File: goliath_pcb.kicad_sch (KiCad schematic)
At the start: 95 parts, among them IC1 MCT9001, IC2 MCT9001, IC3 MCT9001, IC4 MCT9001, IC5 MCT9001, IC6 MCT9001, IC7 MCT9001, J1 RJ45_LED, J10 Conn_01x04_Male, J11 Screw_Terminal_01x02, J12 Screw_Terminal_01x02, J13 Screw_Terminal_01x02, J14 Conn_01x02_Male, J15 Conn_01x02_Male, J2 RJ45_LED, J3 RJ45_LED, J4 RJ45_LED, J5 Conn_01x08_Male, J6 Conn_01x08_Male, J7 Conn_01x02_Male, J8 Conn_01x04_Male, J9 Conn_01x04_Male, Q1 STP2N80K5, Q2 STP2N80K5, U1 Pico, U2 LM2592HVT-5.0/NOPB, U3 74HCT244, U4 74HCT244, U5 MCP3008, U6 PCF8574, U7 PCF8574

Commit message: Clean up schematic
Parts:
- renumbered IC1 to OC1, IC2 to OC2, IC3 to OC3, IC4 to OC4, IC5 to OC5, IC6 to OC6, IC7 to OC7
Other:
- note removed: "LOW EMR caps closest to osmc as possible"
- moved on the sheet: C1, C6, C7, D1, D2, D3, D4, D7, D8, J1, J10, J11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

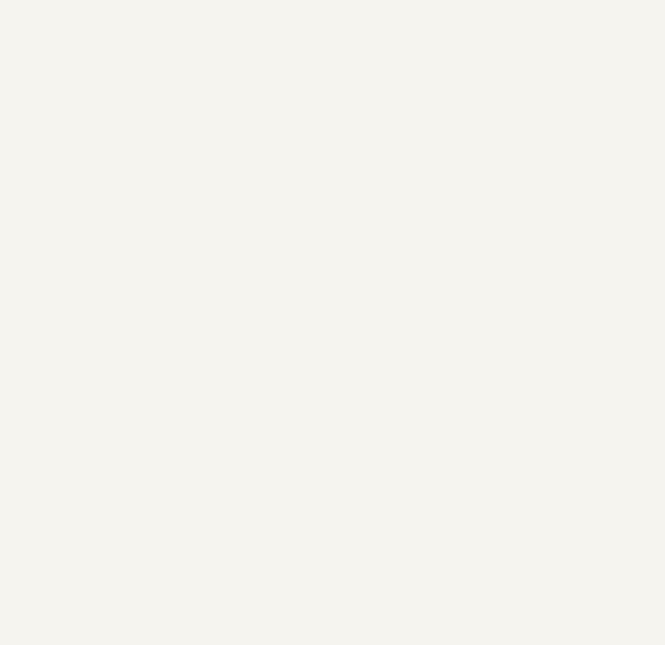
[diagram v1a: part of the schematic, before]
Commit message: Add proper M4 mounting holes
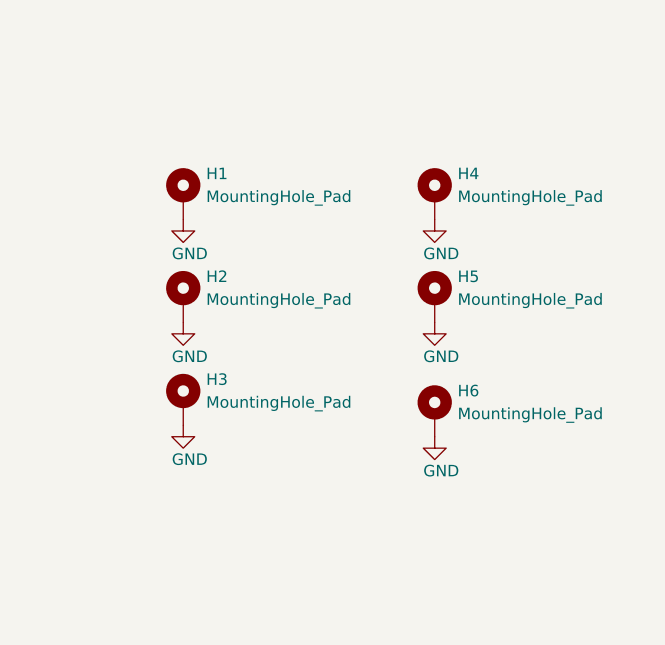
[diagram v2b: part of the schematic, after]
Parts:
- added H1, H2, H3, H4, H5, H6: MountingHole_Pad, MountingHole:MountingHole_4.3mm_M4_Pad_Via, symbol Mechanical:MountingHole_Pad
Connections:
- net GND: now also H1.1, H2.1, H3.1, H4.1, H5.1, H6.1

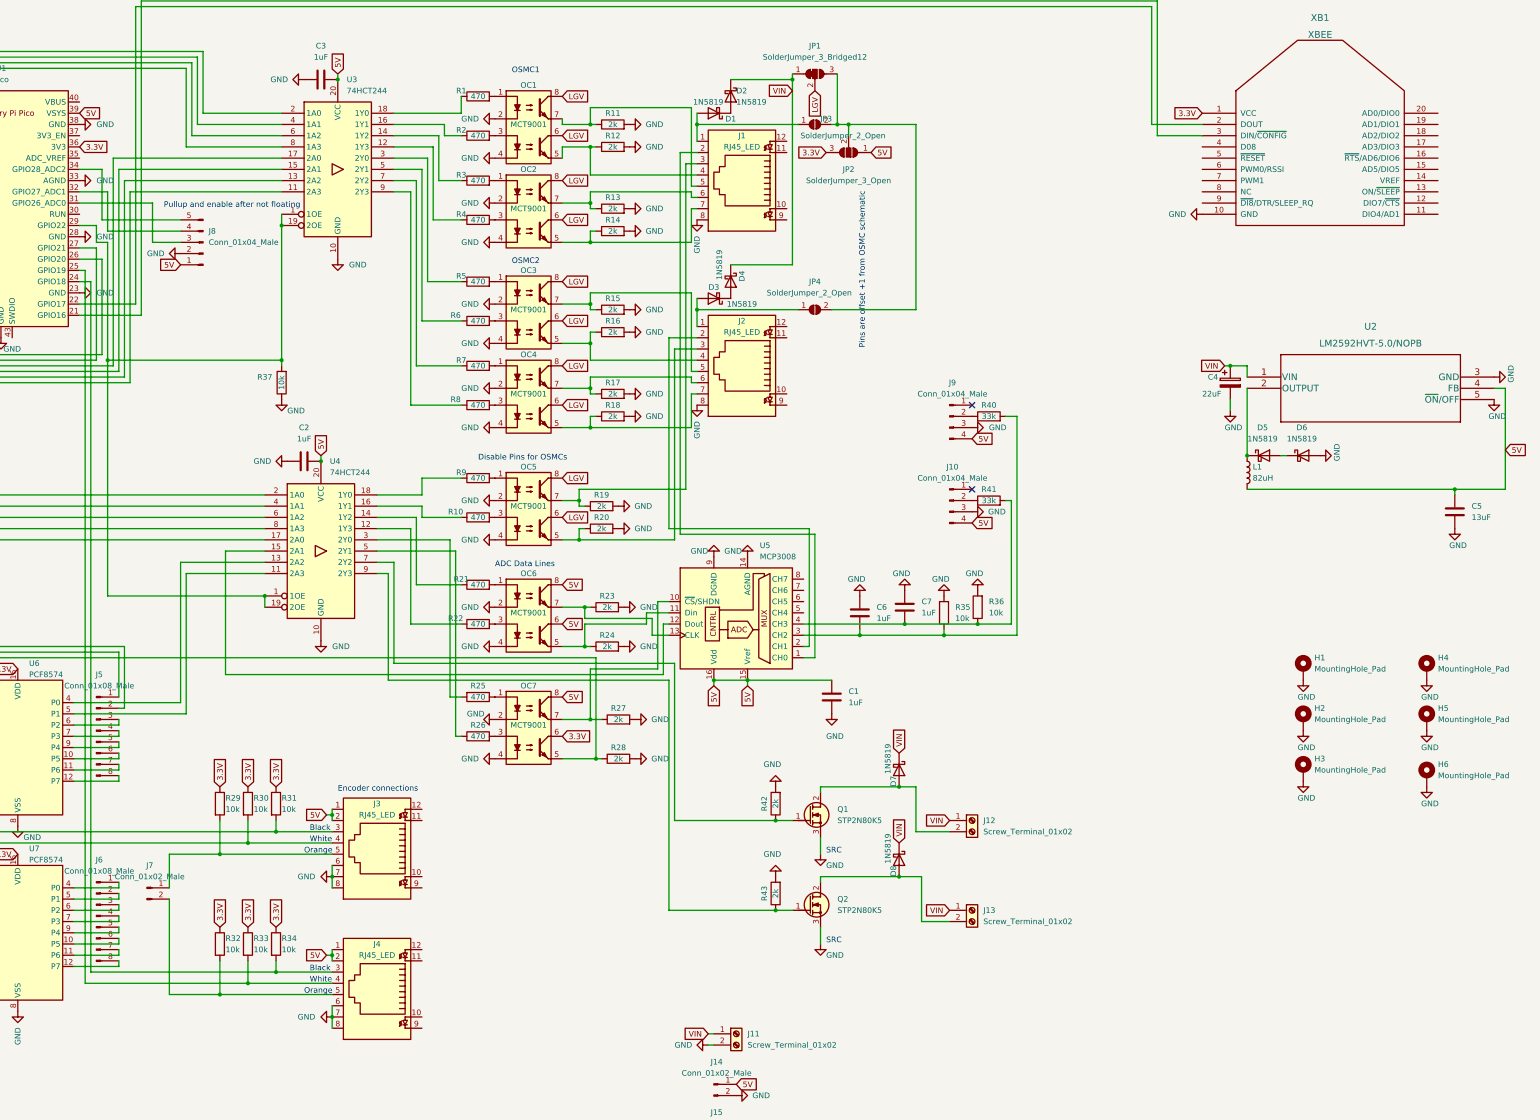
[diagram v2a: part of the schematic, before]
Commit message: Switch to better diodes, use via stitching plugin
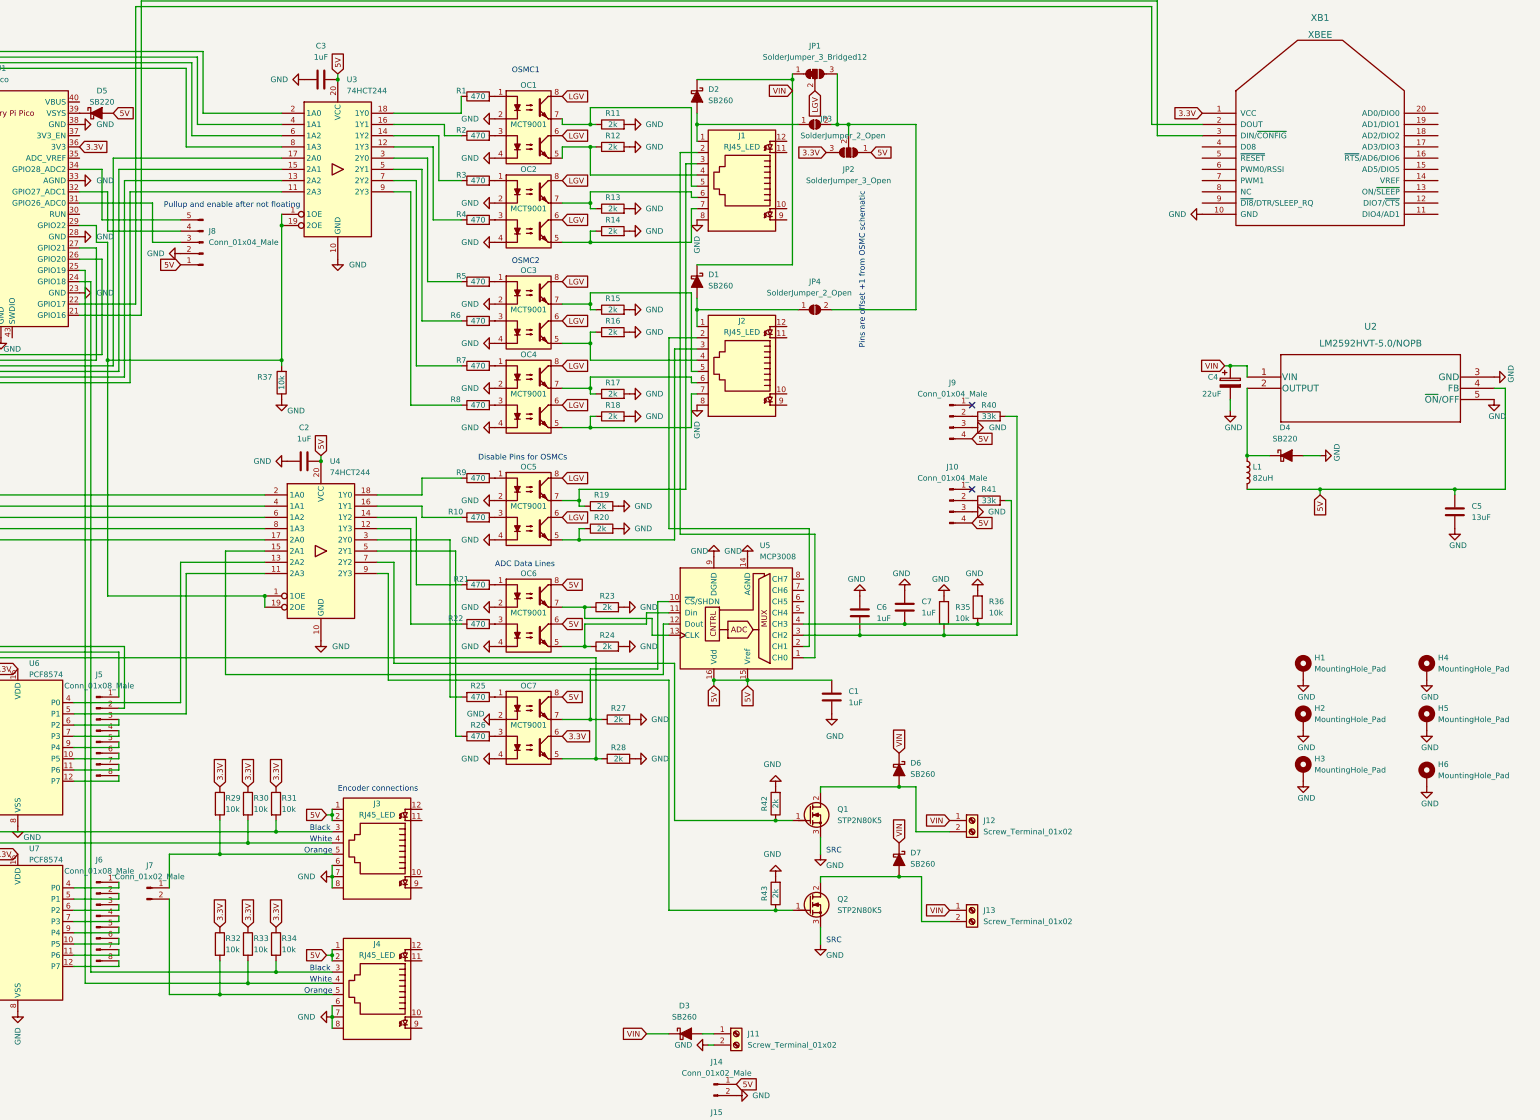
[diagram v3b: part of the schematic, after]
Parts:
- removed D1, D2, D3, D4, D5, D6, D7, D8: 1N5819, Diode_THT:D_DO-41_SOD81_P10.16mm_Horizontal, symbol Diode:1N5819
- added D1, D2, D3, D6, D7: SB260, Diode_THT_AKL:D_DO-15_P10.16mm_Horizontal, symbol Diode_Schottky_AKL:SB260
- added D4, D5: SB220, Diode_THT_AKL:D_DO-15_P10.16mm_Horizontal, symbol Diode_Schottky_AKL:SB220
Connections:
- net 5V: now also D5.2 (A); no longer U1.39 (VSYS)
- net GND: now also D4.2 (A)
- net VIN: now also D1.1 (K), D2.1 (K), D3.1 (K), D6.1 (K), D7.1 (K); no longer J11.1 (Pin_1)
- net at J12.2 (Pin_2), Q1.2 (D): now also D6.2 (A)
- net at J13.2 (Pin_2), Q2.2 (D): now also D7.2 (A)
- net at J1.1, JP3.1 (A): now also D2.2 (A)
- net at L1.1, U2.2 (OUTPUT): now also D4.1 (K)
- net at J2.1, JP4.1 (A): now also D1.2 (A)
- new net: D3.2 (A), J11.1 (Pin_1)
- new net: D5.1 (K), U1.39 (VSYS)

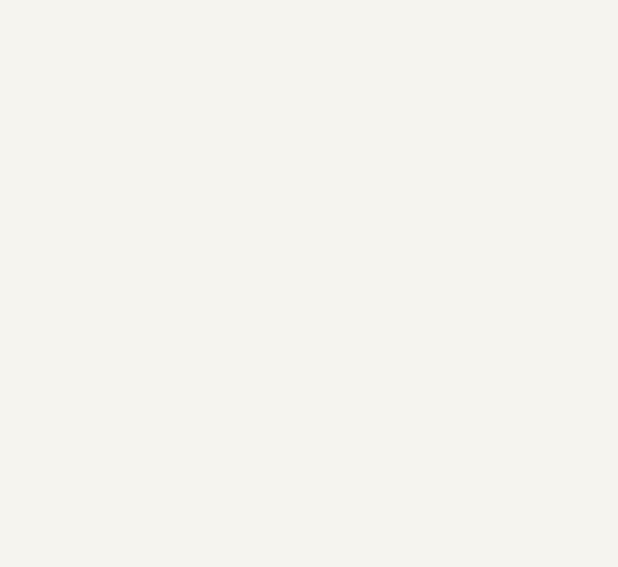
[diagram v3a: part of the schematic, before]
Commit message: Adjust via stitching to alighn with silkscreen text
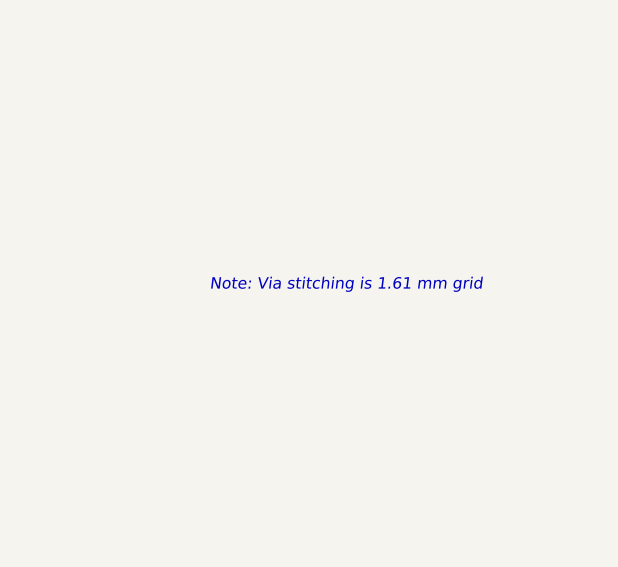
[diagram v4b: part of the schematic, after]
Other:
- note added: "Note: Via stitching is 1.61 mm grid"
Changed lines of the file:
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@@
     (effects (font (size 1.27 1.27)) (justify left bottom))
+  )
+  (text "Note: Via stitching is 1.61 mm grid" (at 370.84 246.38 0)
+    (effects (font (size 1.27 1.27) italic) (justify left bottom))
   )
   (text "Pins are offset +1 from OSMC schematic" (at 250.19 62.23 270)

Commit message: BIG inductor
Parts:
- C4: footprint Capacitor_THT:C_Rect_L7.0mm_W4.5mm_P5.00mm -> Capacitor_THT:CP_Radial_D5.0mm_P2.50mm
- C5: value 13uF -> 10uF
- L1: value 82uH -> 120uH; footprint Inductor_THT:L_Axial_L6.6mm_D2.7mm_P10.16mm_Horizontal_Vishay_IM-2 -> Inductor_THT_AKL:L_Radial_D12.5mm_P7.00mm_Fastron_09HCP
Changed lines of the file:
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@@
       (effects (font (size 1.27 1.27)) (justify left))
     )
-    (property "Value" "82uH" (id 1) (at 337.82 126.9999 0)
-      (effects (font (size 1.27 1.27)) (justify left))
-    )
-    (property "Footprint" "Inductor_THT:L_Axial_L6.6mm_D2.7mm_P10.16mm_Horizontal_Vishay_IM-2" (id 2) (at 336.55 125.73 0)
+    (property "Value" "120uH" (id 1) (at 337.82 126.9999 0)
+      (effects (font (size 1.27 1.27)) (justify left))
+    )
+    (property "Footprint" "Inductor_THT_AKL:L_Radial_D12.5mm_P7.00mm_Fastron_09HCP" (id 2) (at 336.55 125.73 0)
       (effects (font (size 1.27 1.27)) hide)
     )
@@
       (effects (font (size 1.27 1.27)) (justify left))
     )
-    (property "Footprint" "Capacitor_THT:C_Rect_L7.0mm_W4.5mm_P5.00mm" (id 2) (at 333.7052 109.22 0)
+    (property "Footprint" "Capacitor_THT:CP_Radial_D5.0mm_P2.50mm" (id 2) (at 333.7052 109.22 0)
       (effects (font (size 1.27 1.27)) hide)
     )
@@
       (effects (font (size 1.27 1.27)) (justify left))
     )
-    (property "Value" "13uF" (id 1) (at 387.35 135.8899 0)
+    (property "Value" "10uF" (id 1) (at 387.35 135.8899 0)
       (effects (font (size 1.27 1.27)) (justify left))
     )
@@
     )
     (path "/acb13b87-e574-4b2c-9fa0-481a55b275f4"
-      (reference "C4") (unit 1) (value "22uF") (footprint "Capacitor_THT:C_Rect_L7.0mm_W4.5mm_P5.00mm")
+      (reference "C4") (unit 1) (value "22uF") (footprint "Capacitor_THT:CP_Radial_D5.0mm_P2.50mm")
     )
     (path "/f1e5e1aa-d5e8-4580-b07c-74df91c7de8f"
-      (reference "C5") (unit 1) (value "13uF") (footprint "Capacitor_THT:C_Rect_L7.0mm_W4.5mm_P5.00mm")
+      (reference "C5") (unit 1) (value "10uF") (footprint "Capacitor_THT:C_Rect_L7.0mm_W4.5mm_P5.00mm")
     )
     (path "/c3cf2e80-bcc4-4f1a-97b6-1147f3bd1daf"
@@
     )
     (path "/988f1dad-6d98-48c9-a5f9-8b3c8fc49edf"
-      (reference "L1") (unit 1) (value "82uH") (footprint "Inductor_THT:L_Axial_L6.6mm_D2.7mm_P10.16mm_Horizontal_Vishay_IM-2")
+      (reference "L1") (unit 1) (value "120uH") (footprint "Inductor_THT_AKL:L_Radial_D12.5mm_P7.00mm_Fastron_09HCP")
     )
     (path "/ca5671af-d549-43bf-bac5-65bba152b15c"

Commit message: Prepare RC1 for purchase
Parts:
- removed D4, D5: SB220, Diode_THT_AKL:D_DO-15_P10.16mm_Horizontal, symbol Diode_Schottky_AKL:SB220
- added D4, D5: SB230, Diode_THT_AKL:D_DO-15_P10.16mm_Horizontal, symbol Diode_Schottky_AKL:SB230
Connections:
- net 5V: now also D5.2 (A)
- net GND: now also D4.2 (A)
- net at L1.1, U2.2 (OUTPUT): now also D4.1 (K)
- net at U1.39 (VSYS): now also D5.1 (K)
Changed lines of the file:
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@@
     (pin "1")
-  )
-  (symbol (lib_id "Diode_Schottky_AKL:SB220") (at 345.44 121.92 180) (unit 1)
-    (in_bom yes) (on_board yes) (fields_autoplaced)
-    (property "Reference" "D4" (id 0) (at 345.1225 115.57 0))
-    (property "Value" "SB220" (id 1) (at 345.1225 118.11 0))
-    (property "Footprint" "Diode_THT_AKL:D_DO-15_P10.16mm_Horizontal" (id 2) (at 345.44 121.92 0)
-      (effects (font (size 1.27 1.27)) hide)
-    )
-    (property "Datasheet" "https://www.tme.eu/Document/cb30ffdfda65a89a6ebecb81f596d748/sb220.pdf" (id 3) (at 345.44 121.92 0)
-      (effects (font (size 1.27 1.27)) hide)
-    )
-    (pin "1")
-    (pin "2")
   )
   (symbol (lib_id "power:GND") (at 196.85 71.12 90) (unit 1)
@@
     (pin "2")
   )
+  (symbol (lib_id "Diode_Schottky_AKL:SB230") (at 345.44 121.92 180) (unit 1)
+    (in_bom yes) (on_board yes) (fields_autoplaced)
+    (property "Reference" "D4" (id 0) (at 345.1225 115.57 0))
+    (property "Value" "SB230" (id 1) (at 345.1225 118.11 0))
+    (property "Footprint" "Diode_THT_AKL:D_DO-15_P10.16mm_Horizontal" (id 2) (at 345.44 121.92 0)
+      (effects (font (size 1.27 1.27)) hide)
+    )
+    (property "Datasheet" "https://www.tme.eu/Document/cb30ffdfda65a89a6ebecb81f596d748/sb220.pdf" (id 3) (at 345.44 121.92 0)
+      (effects (font (size 1.27 1.27)) hide)
+    )
+    (pin "1")
+    (pin "2")
+  )
   (symbol (lib_id "Device:R") (at 190.5 138.43 90) (unit 1)
     (in_bom yes) (on_board yes)
@@
     (pin "1")
   )
-  (symbol (lib_id "Diode_Schottky_AKL:SB220") (at 76.2 44.45 180) (unit 1)
-    (in_bom yes) (on_board yes)
-    (property "Reference" "D5" (id 0) (at 77.47 39.37 0))
-    (property "Value" "SB220" (id 1) (at 77.47 41.91 0))
-    (property "Footprint" "Diode_THT_AKL:D_DO-15_P10.16mm_Horizontal" (id 2) (at 76.2 44.45 0)
-      (effects (font (size 1.27 1.27)) hide)
-    )
-    (property "Datasheet" "https://www.tme.eu/Document/cb30ffdfda65a89a6ebecb81f596d748/sb220.pdf" (id 3) (at 76.2 44.45 0)
-      (effects (font (size 1.27 1.27)) hide)
-    )
-    (pin "1")
-    (pin "2")
-  )
   (symbol (lib_id "Diode_Schottky_AKL:SB260") (at 257.81 213.36 90) (unit 1)
     (in_bom yes) (on_board yes) (fields_autoplaced)
@@
     )
     (pin "1")
+  )
+  (symbol (lib_id "Diode_Schottky_AKL:SB230") (at 76.2 44.45 180) (unit 1)
+    (in_bom yes) (on_board yes) (fields_autoplaced)
+    (property "Reference" "D5" (id 0) (at 75.8825 38.1 0))
+    (property "Value" "SB230" (id 1) (at 75.8825 40.64 0))
+    (property "Footprint" "Diode_THT_AKL:D_DO-15_P10.16mm_Horizontal" (id 2) (at 76.2 44.45 0)
+      (effects (font (size 1.27 1.27)) hide)
+    )
+    (property "Datasheet" "https://www.tme.eu/Document/cb30ffdfda65a89a6ebecb81f596d748/sb220.pdf" (id 3) (at 76.2 44.45 0)
+      (effects (font (size 1.27 1.27)) hide)
+    )
+    (pin "1")
+    (pin "2")
   )
   (symbol (lib_id "Device:R") (at 162.56 160.02 90) (unit 1)
@@
       (reference "D3") (unit 1) (value "SB260") (footprint "Diode_THT_AKL:D_DO-15_P10.16mm_Horizontal")
     )
-    (path "/23795688-ff9a-4f96-b638-d947ad7bb3cb"
-      (reference "D4") (unit 1) (value "SB220") (footprint "Diode_THT_AKL:D_DO-15_P10.16mm_Horizontal")
-    )
-    (path "/777fb833-3296-4ac5-b344-074dcb552435"
-      (reference "D5") (unit 1) (value "SB220") (footprint "Diode_THT_AKL:D_DO-15_P10.16mm_Horizontal")
+    (path "/3ed48eaf-3578-45b9-91a5-ec4833ee035e"
+      (reference "D4") (unit 1) (value "SB230") (footprint "Diode_THT_AKL:D_DO-15_P10.16mm_Horizontal")
+    )
+    (path "/a1fd9195-4c69-4c70-9d43-5e55c8cee058"
+      (reference "D5") (unit 1) (value "SB230") (footprint "Diode_THT_AKL:D_DO-15_P10.16mm_Horizontal")
     )
     (path "/18a88649-a85c-4384-83ff-9bd04ac0f3c0"

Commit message: Add a reset button, plan for power switch
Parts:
- added SW1: SW_Push, 4.5mm_button:SW_Tactile_PUSH_4.5mm_H3.8mm_TS_C016, symbol Switch:SW_Push
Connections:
- net GND: now also SW1.2
- net at U1.30 (RUN): now also SW1.1
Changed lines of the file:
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@@
     (stroke (width 0) (type default) (color 0 0 0 0))
   )
+  (wire (pts (xy 87.63 67.31) (xy 87.63 86.36))
+    (stroke (width 0) (type default) (color 0 0 0 0))
+  )
   (wire (pts (xy 152.4 68.58) (xy 158.75 68.58))
     (stroke (width 0) (type default) (color 0 0 0 0))
@@
     (stroke (width 0) (type default) (color 0 0 0 0))
   )
+  (wire (pts (xy 72.39 67.31) (xy 87.63 67.31))
+    (stroke (width 0) (type default) (color 0 0 0 0))
+  )
   (wire (pts (xy 29.21 67.31) (xy 29.21 130.81))
     (stroke (width 0) (type default) (color 0 0 0 0))
@@
     (stroke (width 0) (type default) (color 0 0 0 0))
   )
+  (wire (pts (xy 87.63 86.36) (xy 100.33 86.36))
+    (stroke (width 0) (type default) (color 0 0 0 0))
+  )
   (wire (pts (xy 187.96 181.61) (xy 190.5 181.61))
     (stroke (width 0) (type default) (color 0 0 0 0))
@@
     (pin "1")
   )
+  (symbol (lib_id "Switch:SW_Push") (at 105.41 86.36 0) (unit 1)
+    (in_bom yes) (on_board yes) (fields_autoplaced)
+    (property "Reference" "SW1" (id 0) (at 105.41 78.74 0))
+    (property "Value" "SW_Push" (id 1) (at 105.41 81.28 0))
+    (property "Footprint" "4.5mm_button:SW_Tactile_PUSH_4.5mm_H3.8mm_TS_C016" (id 2) (at 105.41 81.28 0)
+      (effects (font (size 1.27 1.27)) hide)
+    )
+    (property "Datasheet" "~" (id 3) (at 105.41 81.28 0)
+      (effects (font (size 1.27 1.27)) hide)
+    )
+    (pin "1")
+    (pin "2")
+  )
   (symbol (lib_id "power:GND") (at 166.37 165.1 270) (unit 1)
     (in_bom yes) (on_board yes)
@@
     (pin "9")
   )
+  (symbol (lib_id "power:GND") (at 110.49 86.36 90) (unit 1)
+    (in_bom yes) (on_board yes)
+    (property "Reference" "#PWR046" (id 0) (at 116.84 86.36 0)
+      (effects (font (size 1.27 1.27)) hide)
+    )
+    (property "Value" "GND" (id 1) (at 118.11 86.36 90)
+      (effects (font (size 1.27 1.27)) (justify left))
+    )
+    (property "Footprint" "" (id 2) (at 110.49 86.36 0)
+      (effects (font (size 1.27 1.27)) hide)
+    )
+    (property "Datasheet" "" (id 3) (at 110.49 86.36 0)
+      (effects (font (size 1.27 1.27)) hide)
+    )
+    (pin "1")
+  )
   (symbol (lib_id "power:GND") (at 26.67 72.39 270) (unit 1)
     (in_bom yes) (on_board yes)
@@
       (reference "#PWR045") (unit 1) (value "GND") (footprint "")
     )
+    (path "/d108e504-ddd4-41da-b6c5-eacdb236fcd6"
+      (reference "#PWR046") (unit 1) (value "GND") (footprint "")
+    )
     (path "/20b3c90c-cd19-43ab-add4-d9614137be68"
       (reference "#PWR0101") (unit 1) (value "GND") (footprint "")
@@
       (reference "R43") (unit 1) (value "2k") (footprint "Resistor_THT:R_Axial_DIN0207_L6.3mm_D2.5mm_P10.16mm_Horizontal")
     )
+    (path "/36a02a4f-b156-458b-b7ce-084cd38c9f3a"
+      (reference "SW1") (unit 1) (value "SW_Push") (footprint "4.5mm_button:SW_Tactile_PUSH_4.5mm_H3.8mm_TS_C016")
+    )
     (path "/cb20d2a1-05a5-401a-9981-368013b11a84"
